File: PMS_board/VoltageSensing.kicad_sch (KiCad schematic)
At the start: 60 parts, among them J18 BAT_SENSE1, J19 BAT_SENSE2, U16 LM324DR, U17 LM324DR, U24 EG6201

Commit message: New current sensor using old op amp
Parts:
- removed unit 3 of U17
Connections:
- no-connect marks 3 -> 0
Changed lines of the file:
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@@
 		(color 0 0 0 0)
 	)
-	(no_connect
-		(at 193.04 119.38)
-	)
-	(no_connect
-		(at 193.04 124.46)
-	)
-	(no_connect
-		(at 208.28 121.92)
-	)
 	(wire
 		(pts
@@
 				)
 			)
-		)
-	)
-	(symbol
-		(lib_id "Amplifier_Operational:Opamp_Quad")
-		(at 200.66 121.92 0)
-		(unit 3)
-		(body_style 1)
-		(exclude_from_sim no)
-		(in_bom yes)
-		(on_board yes)
-		(in_pos_files yes)
-		(dnp no)
-		(fields_autoplaced yes)
-		(property "Reference" "U17"
-			(at 200.66 111.76 0)
-			(show_name no)
-			(do_not_autoplace no)
-			(effects
-				(font
-					(size 1.27 1.27)
-				)
-			)
-		)
-		(property "Value" "LM324DR"
-			(at 200.66 114.3 0)
-			(show_name no)
-			(do_not_autoplace no)
-			(effects
-				(font
-					(size 1.27 1.27)
-				)
-			)
-		)
-		(property "Footprint" "Package_SO:SOIC-14_3.9x8.7mm_P1.27mm"
-			(at 200.66 121.92 0)
-			(hide yes)
-			(show_name no)
-			(do_not_autoplace no)
-			(effects
-				(font
-					(size 1.27 1.27)
-				)
-			)
-		)
-		(property "Datasheet" "https://www.ti.com/lit/ds/symlink/lm224.pdf?HQS=dis-dk-null-digikeymode-dsf-pf-null-wwe&ts=1792150070369"
-			(at 200.66 121.92 0)
-			(hide yes)
-			(show_name no)
-			(do_not_autoplace no)
-			(effects
-				(font
-					(size 1.27 1.27)
-				)
-			)
-		)
-		(property "Description" "Quad operational amplifier"
-			(at 200.66 130.81 0)
-			(hide yes)
-			(show_name no)
-			(do_not_autoplace no)
-			(effects
-				(font
-					(size 1.27 1.27)
-				)
-			)
-		)
-		(property "Sim.Library" "${KICAD10_SYMBOL_DIR}/Simulation_SPICE.sp"
-			(at 187.96 134.62 0)
-			(hide yes)
-			(show_name yes)
-			(do_not_autoplace no)
-			(effects
-				(font
-					(size 1.27 1.27)
-				)
-				(justify left)
-			)
-		)
-		(property "Sim.Name" "kicad_builtin_opamp_quad"
-			(at 187.96 142.24 0)
-			(hide yes)
-			(show_name yes)
-			(do_not_autoplace no)
-			(effects
-				(font
-					(size 1.27 1.27)
-				)
-				(justify left)
-			)
-		)
-		(property "Sim.Device" "SUBCKT"
-			(at 187.96 139.7 0)
-			(hide yes)
-			(show_name yes)
-			(do_not_autoplace no)
-			(effects
-				(font
-					(size 1.27 1.27)
-				)
-				(justify left)
-			)
-		)
-		(property "Sim.Pins" "1=out1 2=in1- 3=in1+ 4=vcc 5=in2+ 6=in2- 7=out2 8=out3 9=in3- 10=in3+ 11=vee 12=in4+ 13=in4- 14=out4"
-			(at 187.96 137.16 0)
-			(hide yes)
-			(show_name yes)
-			(do_not_autoplace no)
-			(effects
-				(font
-					(size 1.27 1.27)
-				)
-				(justify left)
-			)
-		)
-		(property private "KLC_S3.1" "Units A+B are centered, UnitC has a offset so it fits nicely on A or B."
-			(at 187.96 146.05 0)
-			(hide yes)
-			(show_name yes)
-			(do_not_autoplace no)
-			(effects
-				(font
-					(size 1.27 1.27)
-				)
-				(justify left)
-			)
-		)
-		(property private "KLC_S4.1" "Pin1 and Pin7 are the output, adding a name would look ugly and does not add a benefit."
-			(at 187.96 148.59 0)
-			(hide yes)
-			(show_name yes)
-			(do_not_autoplace no)
-			(effects
-				(font
-					(size 1.27 1.27)
-				)
-				(justify left)
-			)
-		)
-		(property private "KLC_S6.2" "This is a generic symbol and thus has no datasheet."
-			(at 187.96 151.13 0)
-			(hide yes)
-			(show_name yes)
-			(do_not_autoplace no)
-			(effects
-				(font
-					(size 1.27 1.27)
-				)
-				(justify left)
-			)
-		)
-		(pin "13"
-		)
-		(pin "3"
-		)
-		(pin "5"
-		)
-		(pin "9"
-		)
-		(pin "12"
-		)
-		(pin "7"
-		)
-		(pin "8"
-		)
-		(pin "14"
-		)
-		(pin "6"
-		)
-		(pin "10"
-		)
-		(pin "11"
-		)
-		(pin "1"
-		)
-		(pin "2"
-		)
-		(pin "4"
-		)
-		(instances
-			(project "PMS_board"
-				(path "/282246b0-e0d8-4997-b3ee-58bf10355d52/9c22a642-2f25-4e63-ae47-811bedacdc79"
-					(reference "U17")
-					(unit 3)
-				)
-			)

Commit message: Fixed references
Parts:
- renumbered D33 to D3, D32 to D4, D31 to D5, D30 to D6, D29 to D7, D28 to D8, D34 to D9, J18 to J2, J19 to J3, R55 to R10, R50 to R11, R51 to R12, R46 to R13, R47 to R14, R48 to R15, R49 to R16, R52 to R17, R53 to R18, R60 to R19, R61 to R20, R56 to R21, R57 to R22, R62 to R23, R63 to R24, R64 to R25, R65 to R26, R66 to R27, R84 to R28, R85 to R29, R86 to R30, R104 to R31, R105 to R32, R103 to R33, R45 to R34, R39 to R35, R15 to R36, R87 to R37, R88 to R38, R90 to R39, R89 to R40, R21 to R41, R58 to R7, R59 to R8, R54 to R9, TP34 to TP1, TP25 to TP10, TP24 to TP11, TP23 to TP12, TP35 to TP13, TP33 to TP2, TP32 to TP3, TP31 to TP4, TP30 to TP5, TP29 to TP6, TP28 to TP7, TP36 to TP8, TP26 to TP9, U16 to U1, U17 to U1, U17 to U2, U16 to U2, U24 to U3

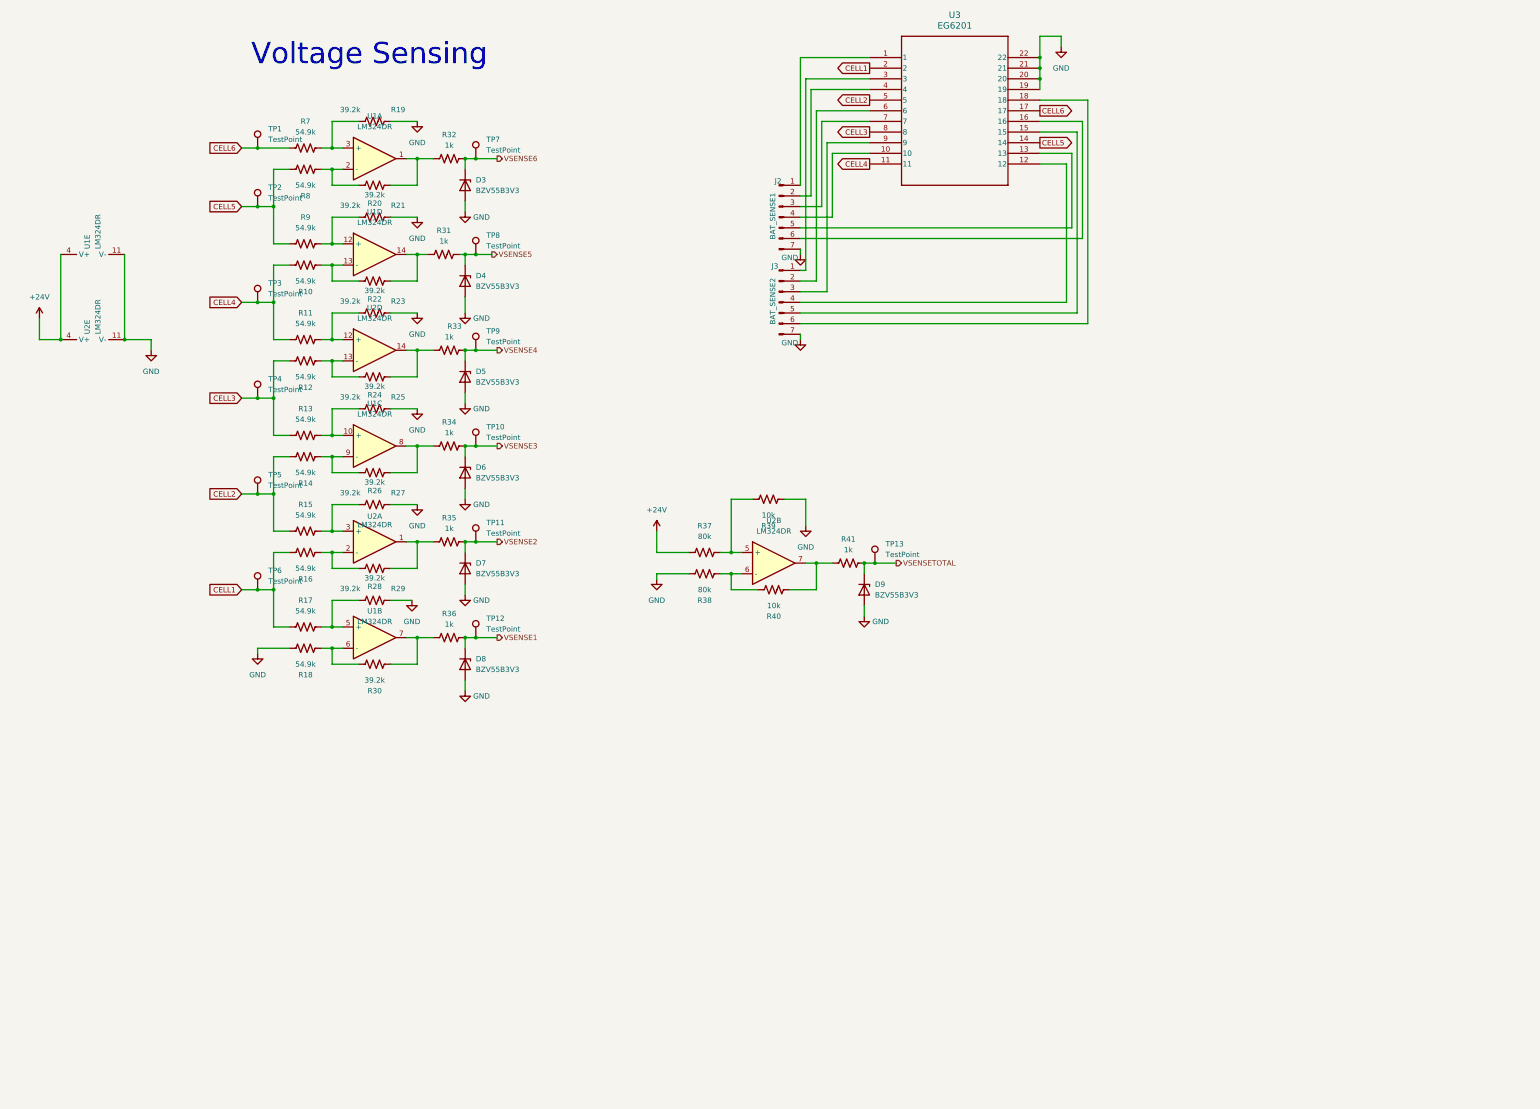
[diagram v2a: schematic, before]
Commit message: Condensed Voltage Sensing circuit
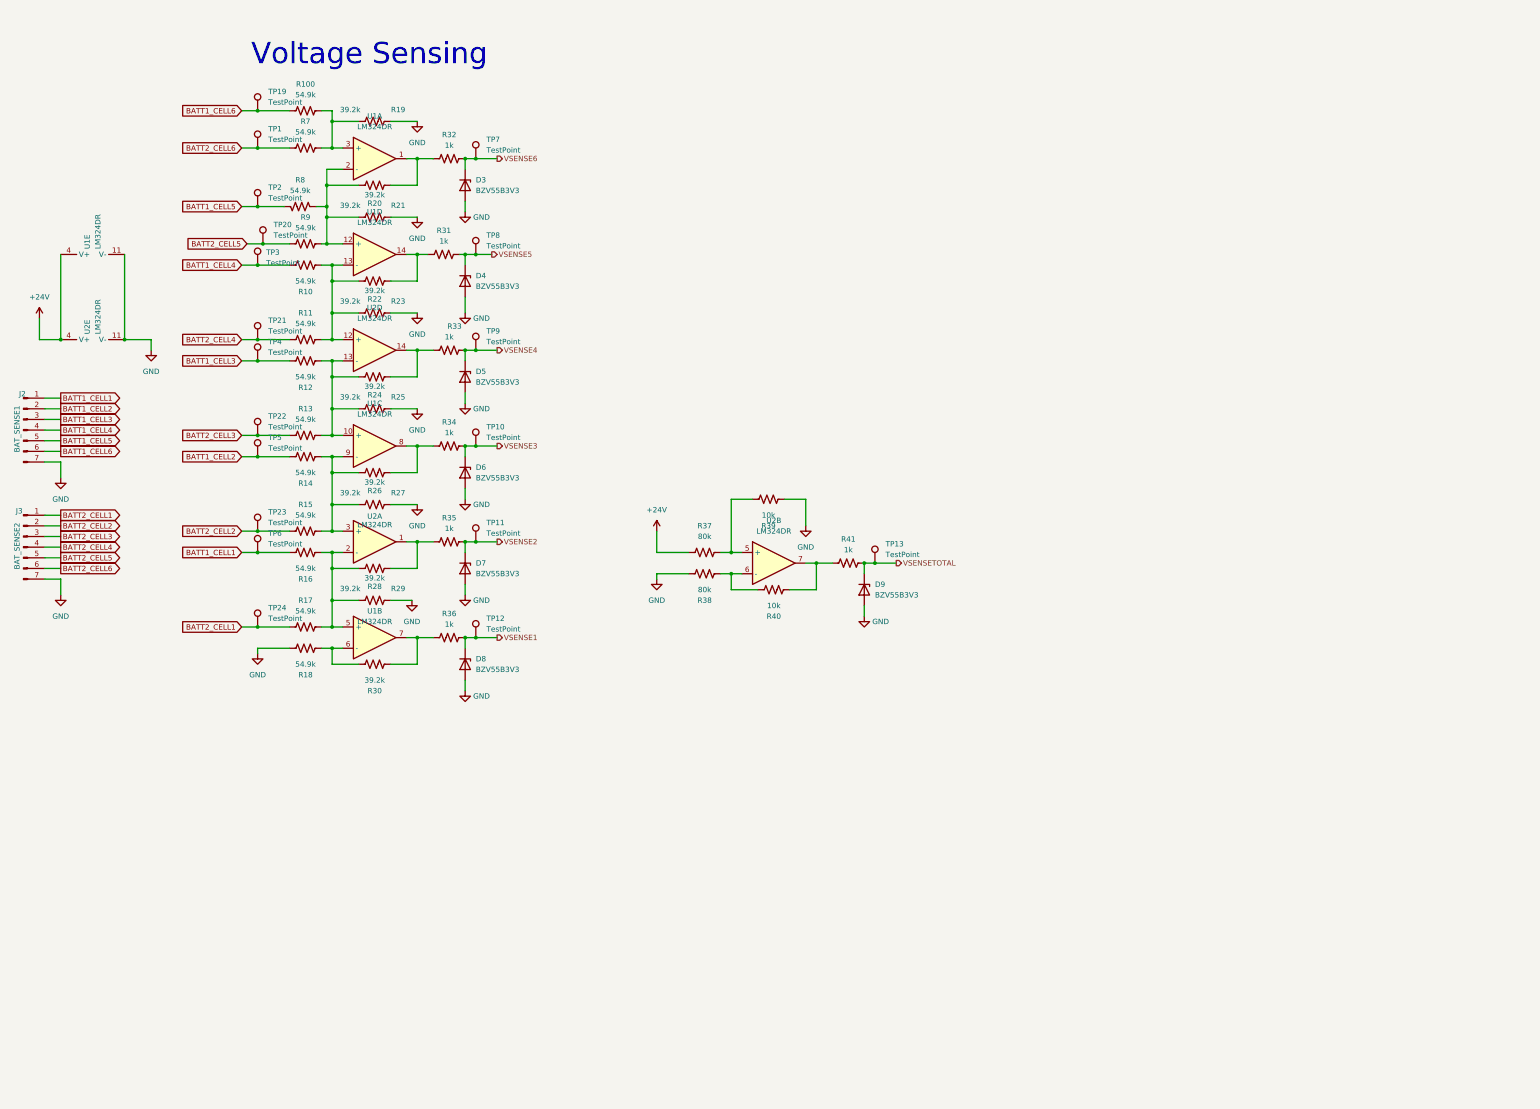
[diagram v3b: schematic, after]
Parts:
- removed U3: EG6201, EG6201:DIP_G6201_EWI, symbol EG6201:EG6201
- added R100: 54.9k, Resistor_SMD:R_0603_1608Metric_Pad0.98x0.95mm_HandSolder, symbol Device:R_US
- added TP19, TP20, TP21, TP22, TP23, TP24: TestPoint, TestPoint:TestPoint_Pad_D1.0mm, symbol Connector:TestPoint
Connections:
- net CELL6 is gone; now on net BATT2_CELL6: R7.1, TP1.1
- net at R15.2, R27.2, U2.3 (+): now also R14.1, R26.1, U1.9 (-)
- net at R19.2, R7.2, U1.3 (+): now also R100.2
- net at R11.2, R23.2, U2.12 (+): now also R10.1, R22.1, U1.13 (-)
- net BATT1_CELL1: now reaches J2.1 (Pin_1)
- net BATT1_CELL1: now also R16.2, TP6.1
- net BATT1_CELL4: now reaches J2.4 (Pin_4)
- net BATT1_CELL4: now also R10.2, TP3.1
- net BATT2_CELL4: now reaches J3.4 (Pin_4)
- net BATT2_CELL4: now also R11.1, TP21.1
- net BATT1_CELL5: now reaches J2.5 (Pin_5)
- net BATT1_CELL5: now also R8.2, TP2.1
- net BATT2_CELL5: now reaches J3.5 (Pin_5)
- net BATT2_CELL5: now also R9.1, TP20.1
- net BATT1_CELL6: now reaches J2.6 (Pin_6)
- net BATT1_CELL6: now also R100.1, TP19.1
- net BATT2_CELL6: now reaches J3.6 (Pin_6)
- net BATT2_CELL1: now reaches J3.1 (Pin_1)
- net BATT2_CELL1: now also R17.1, TP24.1
- net BATT1_CELL2: now reaches J2.2 (Pin_2)
- net BATT1_CELL2: now also R14.2, TP5.1
- net BATT2_CELL2: now reaches J3.2 (Pin_2)
- net BATT2_CELL2: now also R15.1, TP23.1
- net BATT1_CELL3: now reaches J2.3 (Pin_3)
- net BATT1_CELL3: now also R12.2, TP4.1
- net BATT2_CELL3: now reaches J3.3 (Pin_3)
- net BATT2_CELL3: now also R13.1, TP22.1
- net at R20.1, R8.1, U1.2 (-): now also R21.2, R9.2, U1.12 (+)
- net at R12.1, R24.1, U2.13 (-): now also R13.2, R25.2, U1.10 (+)
- net at R17.2, R29.2, U1.5 (+): now also R16.1, R28.1, U2.2 (-)
- removed net CELL1: R16.2, R17.1, TP6.1
- removed net CELL2: R14.2, R15.1, TP5.1
- removed net CELL3: R12.2, R13.1, TP4.1
- removed net CELL4: R10.2, R11.1, TP3.1
- removed net CELL5: R8.2, R9.1, TP2.1
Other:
- moved on the sheet: R8, TP3, TP4

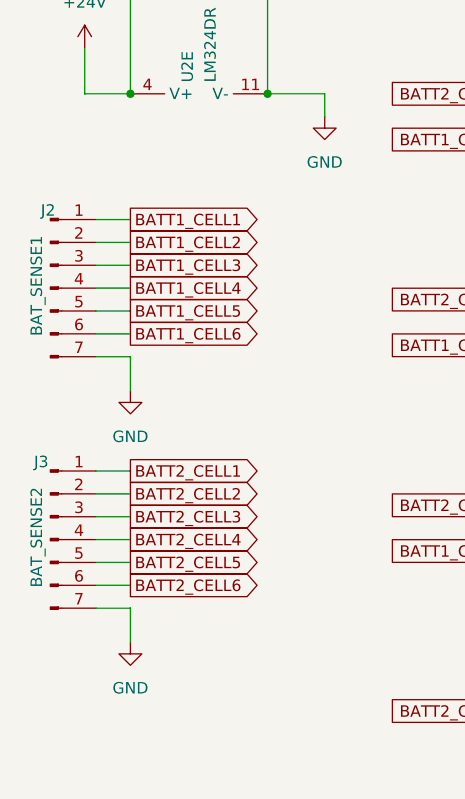
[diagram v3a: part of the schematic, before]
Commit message: Footprints for connectors and new resistors
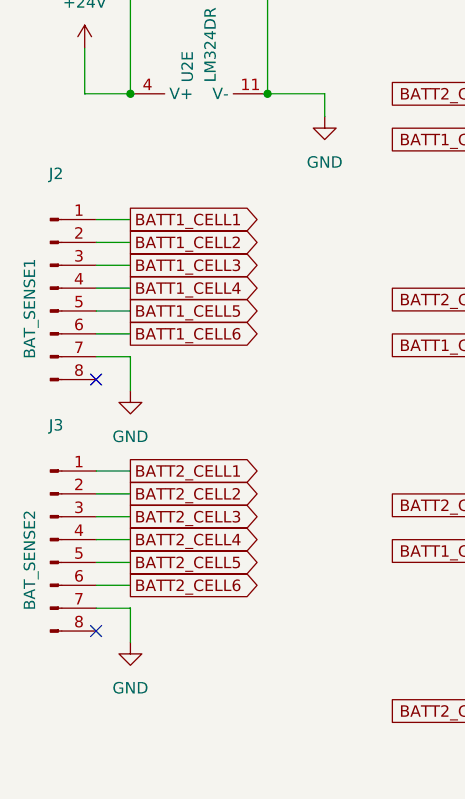
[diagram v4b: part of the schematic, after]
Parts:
- removed J2: BAT_SENSE1, symbol Connector:Conn_01x07_Pin
- removed J3: BAT_SENSE2, symbol Connector:Conn_01x07_Pin
- added J2: BAT_SENSE1, Connector_JST:JST_PH_B8B-PH-K_1x08_P2.00mm_Vertical, symbol Connector:Conn_01x08_Pin
- added J3: BAT_SENSE2, Connector_JST:JST_PH_B8B-PH-K_1x08_P2.00mm_Vertical, symbol Connector:Conn_01x08_Pin
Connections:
- net BATT1_CELL1: now also J2.1 (Pin_1)
- net BATT1_CELL2: now also J2.2 (Pin_2)
- net BATT1_CELL3: now also J2.3 (Pin_3)
- net BATT1_CELL4: now also J2.4 (Pin_4)
- net BATT1_CELL5: now also J2.5 (Pin_5)
- net BATT1_CELL6: now also J2.6 (Pin_6)
- net BATT2_CELL1: now also J3.1 (Pin_1)
- net BATT2_CELL2: now also J3.2 (Pin_2)
- net BATT2_CELL3: now also J3.3 (Pin_3)
- net BATT2_CELL4: now also J3.4 (Pin_4)
- net BATT2_CELL5: now also J3.5 (Pin_5)
- net BATT2_CELL6: now also J3.6 (Pin_6)
- net GND: now also J2.7 (Pin_7), J3.7 (Pin_7)
- no-connect marks 0 -> 2
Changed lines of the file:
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@@
 		(color 0 0 0 0)
 	)
+	(no_connect
+		(at 26.67 127)
+	)
+	(no_connect
+		(at 26.67 154.94)
+	)
 	(wire
 		(pts
@@
 	)
 	(symbol
+		(lib_id "Connector:Conn_01x08_Pin")
+		(at 21.59 144.78 0)
+		(unit 1)
+		(body_style 1)
+		(exclude_from_sim no)
+		(in_bom yes)
+		(on_board yes)
+		(in_pos_files yes)
+		(dnp no)
+		(property "Reference" "J3"
+			(at 22.225 132.08 0)
+			(show_name no)
+			(do_not_autoplace no)
+			(effects
+				(font
+					(size 1.27 1.27)
+				)
+			)
+		)
+		(property "Value" "BAT_SENSE2"
+			(at 19.304 147.066 90)
+			(show_name no)
+			(do_not_autoplace no)
+			(effects
+				(font
+					(size 1.27 1.27)
+				)
+			)
+		)
+		(property "Footprint" "Connector_JST:JST_PH_B8B-PH-K_1x08_P2.00mm_Vertical"
+			(at 21.59 144.78 0)
+			(hide yes)
+			(show_name no)
+			(do_not_autoplace no)
+			(effects
+				(font
+					(size 1.27 1.27)
+				)
+			)
+		)
+		(property "Datasheet" ""
+			(at 21.59 144.78 0)
+			(hide yes)
+			(show_name no)
+			(do_not_autoplace no)
+			(effects
+				(font
+					(size 1.27 1.27)
+				)
+			)
+		)
+		(property "Description" "Generic connector, single row, 01x08, script generated"
+			(at 21.59 144.78 0)
+			(hide yes)
+			(show_name no)
+			(do_not_autoplace no)
+			(effects
+				(font
+					(size 1.27 1.27)
+				)
+			)
+		)
+		(pin "5"
+		)
+		(pin "7"
+		)
+		(pin "3"
+		)
+		(pin "2"
+		)
+		(pin "1"
+		)
+		(pin "4"
+		)
+		(pin "8"
+		)
+		(pin "6"
+		)
+		(instances
+			(project "PMS_board"
+				(path "/282246b0-e0d8-4997-b3ee-58bf10355d52/9c22a642-2f25-4e63-ae47-811bedacdc79"
+					(reference "J3")
+					(unit 1)
+				)
+			)
+		)
+	)
+	(symbol
 		(lib_id "Diode:BZV55B3V3")
 		(at 127 127 270)
@@
 	)
 	(symbol
+		(lib_id "Connector:Conn_01x08_Pin")
+		(at 21.59 116.84 0)
+		(unit 1)
+		(body_style 1)
+		(exclude_from_sim no)
+		(in_bom yes)
+		(on_board yes)
+		(in_pos_files yes)
+		(dnp no)
+		(property "Reference" "J2"
+			(at 22.225 104.14 0)
+			(show_name no)
+			(do_not_autoplace no)
+			(effects
+				(font
+					(size 1.27 1.27)
+				)
+			)
+		)
+		(property "Value" "BAT_SENSE1"
+			(at 19.304 119.126 90)
+			(show_name no)
+			(do_not_autoplace no)
+			(effects
+				(font
+					(size 1.27 1.27)
+				)
+			)
+		)
+		(property "Footprint" "Connector_JST:JST_PH_B8B-PH-K_1x08_P2.00mm_Vertical"
+			(at 21.59 116.84 0)
+			(hide yes)
+			(show_name no)
+			(do_not_autoplace no)
+			(effects
+				(font
+					(size 1.27 1.27)
+				)
+			)
+		)
+		(property "Datasheet" ""
+			(at 21.59 116.84 0)
+			(hide yes)
+			(show_name no)
+			(do_not_autoplace no)
+			(effects
+				(font
+					(size 1.27 1.27)
+				)
+			)
+		)
+		(property "Description" "Generic connector, single row, 01x08, script generated"
+			(at 21.59 116.84 0)
+			(hide yes)
+			(show_name no)
+			(do_not_autoplace no)
+			(effects
+				(font
+					(size 1.27 1.27)
+				)
+			)
+		)
+		(pin "5"
+		)
+		(pin "7"
+		)
+		(pin "3"
+		)
+		(pin "2"
+		)
+		(pin "1"
+		)
+		(pin "4"
+		)
+		(pin "8"
+		)
+		(pin "6"
+		)
+		(instances
+			(project "PMS_board"
+				(path "/282246b0-e0d8-4997-b3ee-58bf10355d52/9c22a642-2f25-4e63-ae47-811bedacdc79"
+					(reference "J2")
+					(unit 1)
+				)
+			)
+		)
+	)
+	(symbol
 		(lib_id "Connector:TestPoint")
 		(at 77.47 123.19 0)
@@
 	)
 	(symbol
-		(lib_id "Connector:Conn_01x07_Pin")
-		(at 21.59 144.78 0)
-		(unit 1)
-		(body_style 1)
-		(exclude_from_sim no)
-		(in_bom yes)
-		(on_board yes)
-		(in_pos_files yes)
-		(dnp no)
-		(property "Reference" "J3"
-			(at 20.574 136.144 0)
-			(show_name no)
-			(do_not_autoplace no)
-			(effects
-				(font
-					(size 1.27 1.27)
-				)
-			)
-		)
-		(property "Value" "BAT_SENSE2"
-			(at 20.066 144.526 90)
-			(show_name no)
-			(do_not_autoplace no)
-			(effects
-				(font
-					(size 1.27 1.27)
-				)
-			)
-		)
-		(property "Footprint" ""
-			(at 21.59 144.78 0)
-			(hide yes)
-			(show_name no)
-			(do_not_autoplace no)
-			(effects
-				(font
-					(size 1.27 1.27)
-				)
-			)
-		)
-		(property "Datasheet" ""
-			(at 21.59 144.78 0)
-			(hide yes)
-			(show_name no)
-			(do_not_autoplace no)
-			(effects
-				(font
-					(size 1.27 1.27)
-				)
-			)
-		)
-		(property "Description" "Generic connector, single row, 01x07, script generated"
-			(at 21.59 144.78 0)
-			(hide yes)
-			(show_name no)
-			(do_not_autoplace no)
-			(effects
-				(font
-					(size 1.27 1.27)
-				)
-			)
-		)
-		(property "KLC_S3.1" ""
-			(at 21.59 144.78 0)
-			(hide yes)
-			(show_name no)
-			(do_not_autoplace no)
-			(effects
-				(font
-					(size 1.27 1.27)
-				)
-			)
-		)
-		(property "KLC_S4.1" ""
-			(at 21.59 144.78 0)
-			(hide yes)
-			(show_name no)
-			(do_not_autoplace no)
-			(effects
-				(font
-					(size 1.27 1.27)
-				)
-			)
-		)
-		(property "KLC_S6.2" ""
-			(at 21.59 144.78 0)
-			(hide yes)
-			(show_name no)
-			(do_not_autoplace no)
-			(effects
-				(font
-					(size 1.27 1.27)
-				)
-			)
-		)
-		(pin "2"
-		)
-		(pin "4"
-		)
-		(pin "3"
-		)
-		(pin "1"
-		)
-		(pin "5"
-		)
-		(pin "6"
-		)
-		(pin "7"
-		)
-		(instances
-			(project "PMS_board"
-				(path "/282246b0-e0d8-4997-b3ee-58bf10355d52/9c22a642-2f25-4e63-ae47-811bedacdc79"
-					(reference "J3")
-					(unit 1)
-				)
-			)
-		)
-	)
-	(symbol
 		(lib_id "Connector:TestPoint")
 		(at 77.47 63.5 0)
@@
 					(unit 1)
 				)
-			)
-		)
-	)
-	(symbol
-		(lib_id "Connector:Conn_01x07_Pin")
-		(at 21.59 116.84 0)
-		(unit 1)
-		(body_style 1)
-		(exclude_from_sim no)
-		(in_bom yes)
-		(on_board yes)
-		(in_pos_files yes)
-		(dnp no)
-		(property "Reference" "J2"
-			(at 21.336 108.204 0)
-			(show_name no)
-			(do_not_autoplace no)
-			(effects
-				(font
-					(size 1.27 1.27)
-				)
-			)
-		)
-		(property "Value" "BAT_SENSE1"
-			(at 20.066 116.586 90)
-			(show_name no)
-			(do_not_autoplace no)
-			(effects
-				(font
-					(size 1.27 1.27)
-				)
-			)
-		)
-		(property "Footprint" ""
-			(at 21.59 116.84 0)
-			(hide yes)
-			(show_name no)
-			(do_not_autoplace no)
-			(effects
-				(font
-					(size 1.27 1.27)
-				)
-			)
-		)
-		(property "Datasheet" ""
-			(at 21.59 116.84 0)
-			(hide yes)
-			(show_name no)
-			(do_not_autoplace no)
-			(effects
-				(font
-					(size 1.27 1.27)
-				)
-			)
-		)
-		(property "Description" "Generic connector, single row, 01x07, script generated"
-			(at 21.59 116.84 0)
-			(hide yes)
-			(show_name no)
-			(do_not_autoplace no)
-			(effects
-				(font
-					(size 1.27 1.27)
-				)
-			)
-		)
-		(property "KLC_S3.1" ""
-			(at 21.59 116.84 0)
-			(hide yes)
-			(show_name no)
-			(do_not_autoplace no)
-			(effects
-				(font
-					(size 1.27 1.27)
-				)
-			)
-		)
-		(property "KLC_S4.1" ""
-			(at 21.59 116.84 0)
-			(hide yes)
-			(show_name no)
-			(do_not_autoplace no)
-			(effects
-				(font
-					(size 1.27 1.27)
-				)
-			)
-		)
-		(property "KLC_S6.2" ""
-			(at 21.59 116.84 0)
-			(hide yes)
-			(show_name no)
-			(do_not_autoplace no)
-			(effects
-				(font
-					(size 1.27 1.27)
-				)
-			)
-		)
-		(pin "2"
-		)
-		(pin "4"
-		)
-		(pin "3"
-		)
-		(pin "1"
-		)
-		(pin "5"
-		)
-		(pin "6"
-		)
-		(pin "7"
-		)
-		(instances
-			(project "PMS_board"
-				(path "/282246b0-e0d8-4997-b3ee-58bf10355d52/9c22a642-2f25-4e63-ae47-811bedacdc79"
-					(reference "J2")
-					(unit 1)
-				)
